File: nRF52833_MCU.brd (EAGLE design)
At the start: 47.7 x 30.2 mm, 45 parts, among them IC1 SKY13415-485LF, J100 DEBUG_CONNECTOR, J3 282834-2, U1 nRF52833-QIAA, X1 32MHz, X2 32.768kHz, X3 22-23-2031

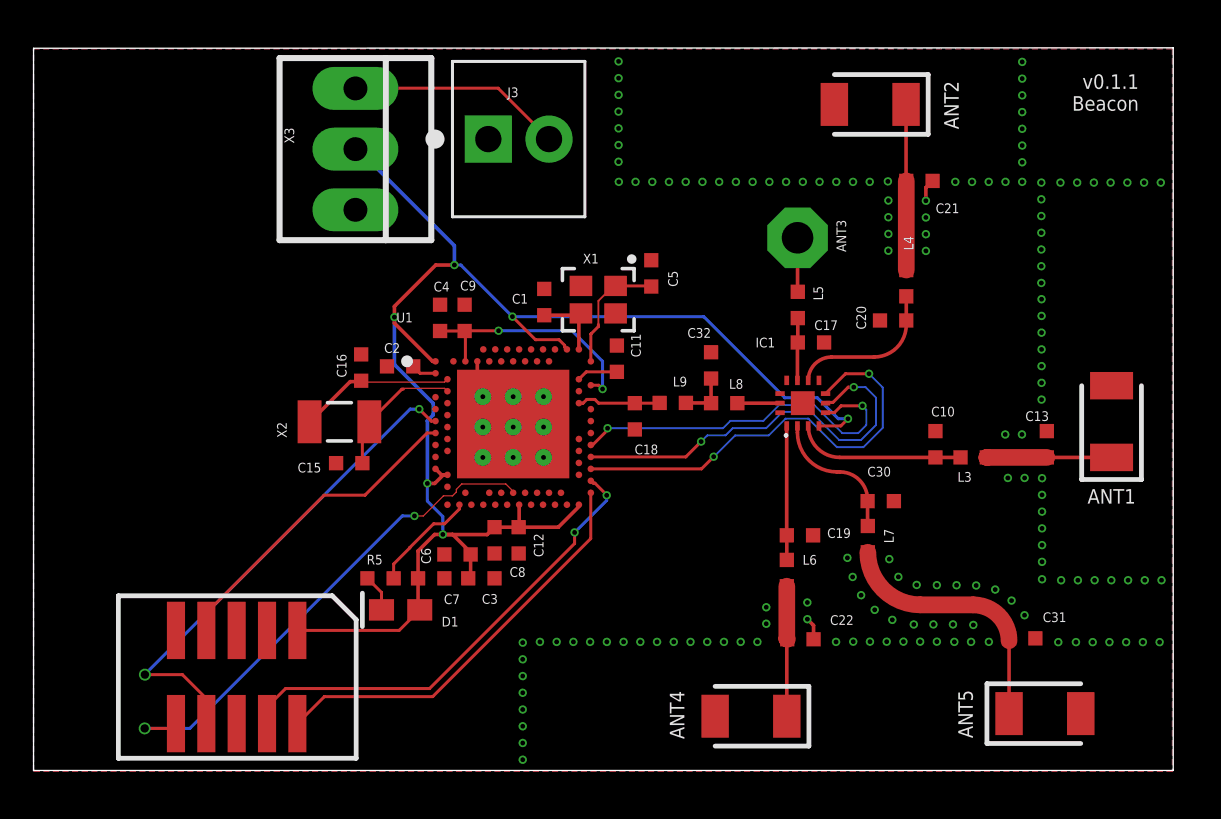
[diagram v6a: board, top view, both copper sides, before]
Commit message: Make sure to respect the design rules
Signed-off-by: Florian Depraz <florian.depraz@outlook.com>
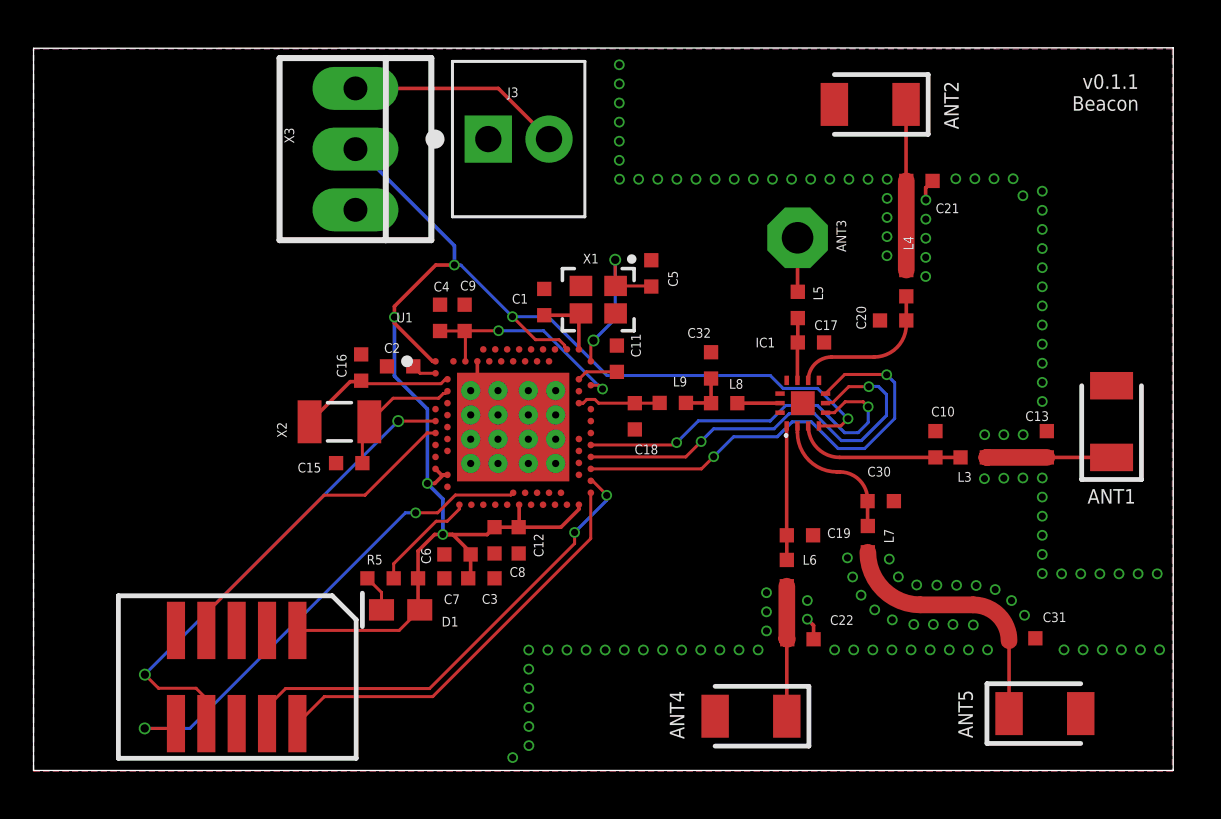
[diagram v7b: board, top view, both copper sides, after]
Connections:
- removed net DECUSB: U1.AC5
- removed net VBUS: U1.AD2
- net GND: now also U1.P$10, U1.P$11, U1.P$12, U1.P$13, U1.P$14, U1.P$15, U1.P$16, U1.P$17, U1.P$18, U1.P$19, U1.P$20; no longer U1.P$6, U1.P$7, U1.P$8, U1.P$9
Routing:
- net XC1: track 5.05 -> 7.28 mm, vias 0 -> 2
- net ANT_SEL_V1: track 18.6 -> 19.4 mm
- net ANT_SEL_V2: track 17.2 -> 17.9 mm
- net DEC6: track 10.3 -> 9.65 mm
- net GND: track 3.47 -> 4.04 mm, vias 34 -> 116
